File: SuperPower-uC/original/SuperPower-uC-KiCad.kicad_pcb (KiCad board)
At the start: 4 copper layers, 92.2 x 45.2 mm, 142 parts, among them J1 JST_PH_S2B_thru, J10 Conn_01x13_Male, J3 Conn_01x02_Male, J4 DNP/JST_ZH_S2B_thru, J5 DNP/JST_XH_S2B_thru, J6 Conn_01x02_Male, J7 Conn_01x14_Male, J8 Conn_01x14_Male, J9 Conn_01x13_Female, Q1 DMN2019UTS, Q10 2N7002A, Q11 2N7002A, Q12 DMP2035UVT, Q13 DMP2035UVT, Q14 DMP2035UVT, Q15 DMN3023L, Q2 Si3421DV, Q3 DMN3023L, Q4 2N7002A, Q5 DMP2035UVT, Q6 BSS84-7-F, Q7 S8050, Q8 S8050, Q9 2N7002A, SW1 DNP/SKRKAEE020, U1 AP9101CK6-AYTRG1, U10 TPS63070RNMT, U2 USB-C, U3 IP4220CZ6, U4 LTC4162EUFD-LAD, U5 RV-3028-C7, U6 CP2102N-A01-GQFN28, U7 ESP32-WROOM32, U8 TPS70933DRVT, U9 TPS63070RNMT

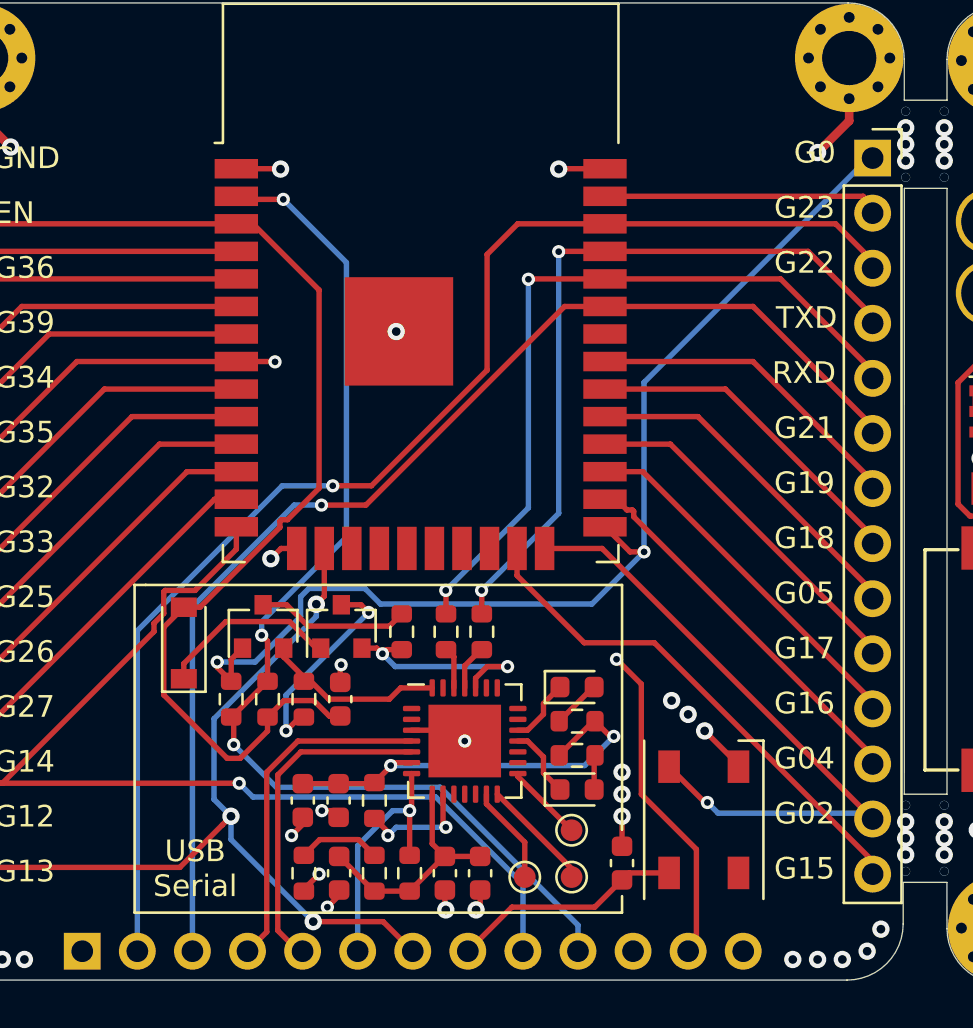
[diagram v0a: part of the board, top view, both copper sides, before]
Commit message: Changed silk text sizes
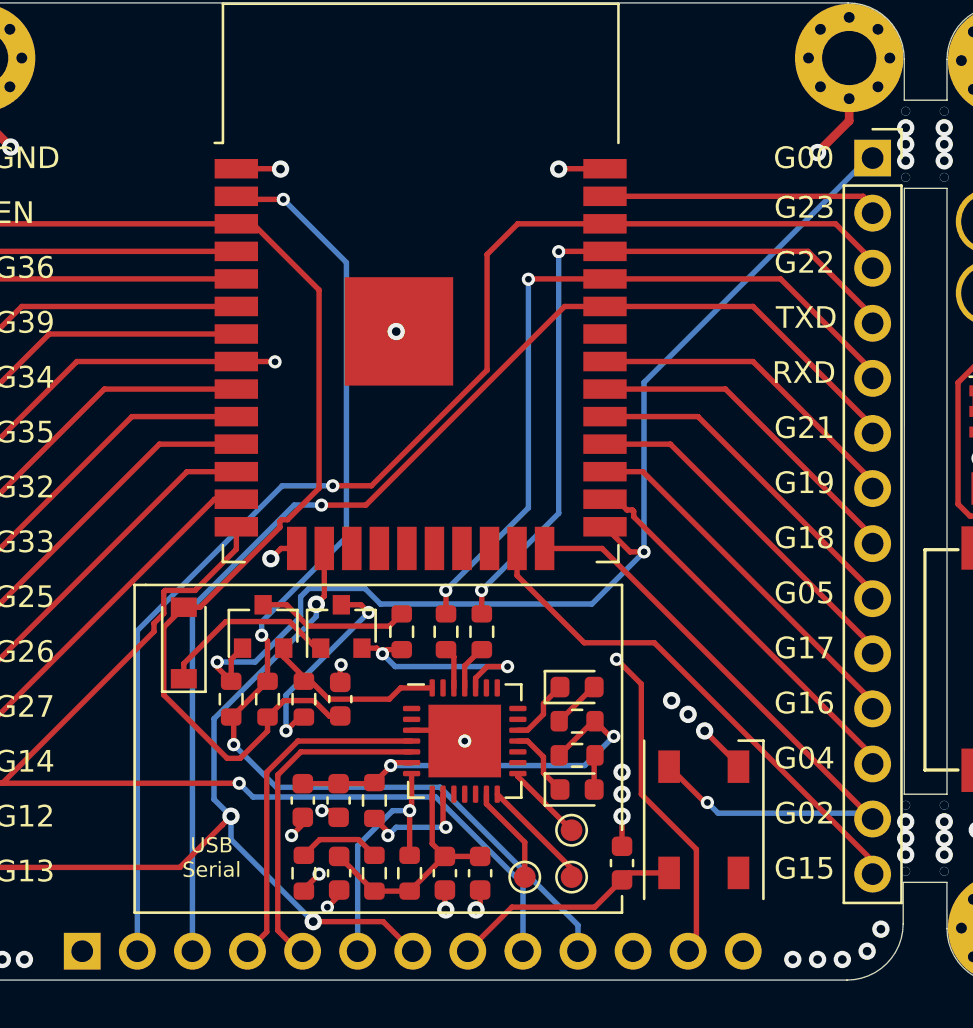
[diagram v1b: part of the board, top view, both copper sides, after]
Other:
- board text added: "G00"
- board text removed: "G0"
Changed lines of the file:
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@@
   (gr_line (start 173.355 76.454) (end 173.355 83.058) (layer F.SilkS) (width 0.12))
   (gr_text VIN (at 160.02 89.662) (layer B.SilkS)
-    (effects (font (size 0.5 0.5) (thickness 0.125)) (justify mirror))
+    (effects (font (size 0.7 0.7) (thickness 0.175)) (justify mirror))
   )
-  (gr_text GND (at 160.02 86.36) (layer B.SilkS)
-    (effects (font (size 0.5 0.5) (thickness 0.125)) (justify mirror))
+  (gr_text GND (at 160.147 86.36) (layer B.SilkS)
+    (effects (font (size 0.7 0.7) (thickness 0.175)) (justify mirror))
   )
-  (gr_text "Battery In" (at 186.69 82.804) (layer B.SilkS)
-    (effects (font (size 0.5 0.5) (thickness 0.125)) (justify mirror))
+  (gr_text "Battery In" (at 185.928 82.804) (layer B.SilkS)
+    (effects (font (size 0.7 0.7) (thickness 0.175)) (justify mirror))
   )
-  (gr_line (start 182.245 82.169) (end 188.722 82.169) (layer B.SilkS) (width 0.12))
-  (gr_line (start 193.167 95.25) (end 186.309 95.25) (layer B.SilkS) (width 0.12))
-  (gr_text "Battery Out" (at 190.246 89.027) (layer B.SilkS)
-    (effects (font (size 0.6 0.6) (thickness 0.125)) (justify mirror))
+  (gr_line (start 181.356 82.169) (end 188.722 82.169) (layer B.SilkS) (width 0.12))
+  (gr_line (start 193.167 95.25) (end 184.785 95.25) (layer B.SilkS) (width 0.12))
+  (gr_text "Battery Out" (at 189.865 88.773) (layer B.SilkS)
+    (effects (font (size 0.7 0.7) (thickness 0.175)) (justify mirror))
   )
-  (gr_line (start 161.29 91.313) (end 161.29 84.201) (layer B.SilkS) (width 0.12))
-  (gr_line (start 153.924 91.313) (end 161.29 91.313) (layer B.SilkS) (width 0.12))
+  (gr_line (start 163.576 91.313) (end 163.576 84.201) (layer B.SilkS) (width 0.12))
+  (gr_line (start 153.924 91.313) (end 163.576 91.313) (layer B.SilkS) (width 0.12))
   (gr_line (start 153.924 84.201) (end 153.924 91.313) (layer B.SilkS) (width 0.12))
-  (gr_line (start 161.29 84.201) (end 153.924 84.201) (layer B.SilkS) (width 0.12))
+  (gr_line (start 163.576 84.201) (end 153.924 84.201) (layer B.SilkS) (width 0.12))
   (gr_line (start 160.02 76.708) (end 160.02 80.899) (layer F.SilkS) (width 0.12))
   (gr_line (start 153.924 76.708) (end 160.02 76.708) (layer F.SilkS) (width 0.12))
@@
     (effects (font (size 0.7 0.7) (thickness 0.175)) (justify mirror))
   )
-  (gr_line (start 188.722 87.503) (end 182.245 87.503) (layer B.SilkS) (width 0.12))
+  (gr_line (start 188.722 87.503) (end 181.356 87.503) (layer B.SilkS) (width 0.12))
   (gr_line (start 188.722 82.169) (end 188.722 87.503) (layer B.SilkS) (width 0.12))
-  (gr_line (start 182.245 87.503) (end 182.245 82.169) (layer B.SilkS) (width 0.12))
-  (gr_line (start 193.167 95.25) (end 193.167 88.265) (layer B.SilkS) (width 0.12))
-  (gr_line (start 186.309 88.265) (end 186.309 95.25) (layer B.SilkS) (width 0.12))
-  (gr_line (start 193.167 88.265) (end 186.309 88.265) (layer B.SilkS) (width 0.12))
-  (gr_text "USB\nSerial" (at 114.046 116.205) (layer F.SilkS)
-    (effects (font (size 1 1) (thickness 0.15)))
+  (gr_line (start 181.356 87.503) (end 181.356 82.169) (layer B.SilkS) (width 0.12))
+  (gr_line (start 193.167 95.25) (end 193.167 88.138) (layer B.SilkS) (width 0.12))
+  (gr_line (start 184.785 88.138) (end 184.785 95.25) (layer B.SilkS) (width 0.12))
+  (gr_line (start 193.167 88.138) (end 184.785 88.138) (layer B.SilkS) (width 0.12))
+  (gr_text "USB\nSerial" (at 114.808 115.697) (layer F.SilkS)
+    (effects (font (size 0.7 0.7) (thickness 0.15)))
   )
   (gr_line (start 111.252 103.124) (end 111.76 103.124) (layer F.SilkS) (width 0.12))
@@
     (effects (font (size 1 1) (thickness 0.15)))
   )
-  (gr_text G0 (at 142.621 83.185) (layer F.SilkS)
+  (gr_text G00 (at 142.113 83.439) (layer F.SilkS)
     (effects (font (size 1 1) (thickness 0.15)))
   )
@@
   (gr_line (start 146.74596 78.87716) (end 146.74596 80.772) (layer Edge.Cuts) (width 0.05))
   (gr_line (start 148.717 80.772) (end 146.74596 80.772) (layer Edge.Cuts) (width 0.05))
-  (gr_text "Power In 5V-20V" (at 157.734 84.709) (layer B.SilkS)
-    (effects (font (size 0.5 0.5) (thickness 0.125)) (justify mirror))
+  (gr_text "Power In 5V-20V" (at 158.75 84.836) (layer B.SilkS)
+    (effects (font (size 0.7 0.7) (thickness 0.175)) (justify mirror))
   )
-  (gr_text GND (at 188.976 93.345) (layer B.SilkS)
-    (effects (font (size 0.5 0.5) (thickness 0.125)) (justify mirror))
+  (gr_text GND (at 188.595 93.345) (layer B.SilkS)
+    (effects (font (size 0.7 0.7) (thickness 0.175)) (justify mirror))
   )
-  (gr_text Battery+ (at 188.087 90.678) (layer B.SilkS)
-    (effects (font (size 0.5 0.5) (thickness 0.125)) (justify mirror))
+  (gr_text Battery+ (at 187.325 90.805) (layer B.SilkS)
+    (effects (font (size 0.7 0.7) (thickness 0.175)) (justify mirror))
   )
-  (gr_text Battery- (at 184.531 84.328) (layer B.SilkS)
-    (effects (font (size 0.5 0.5) (thickness 0.125)) (justify mirror))
+  (gr_text Battery- (at 183.896 84.328) (layer B.SilkS)
+    (effects (font (size 0.7 0.7) (thickness 0.175)) (justify mirror))
   )
-  (gr_text Battery+ (at 184.531 86.36) (layer B.SilkS)
-    (effects (font (size 0.5 0.5) (thickness 0.125)) (justify mirror))
+  (gr_text Battery+ (at 183.896 86.36) (layer B.SilkS)
+    (effects (font (size 0.7 0.7) (thickness 0.175)) (justify mirror))
   )
   (gr_text SCL (at 158.369 117.673429 90) (layer B.SilkS)

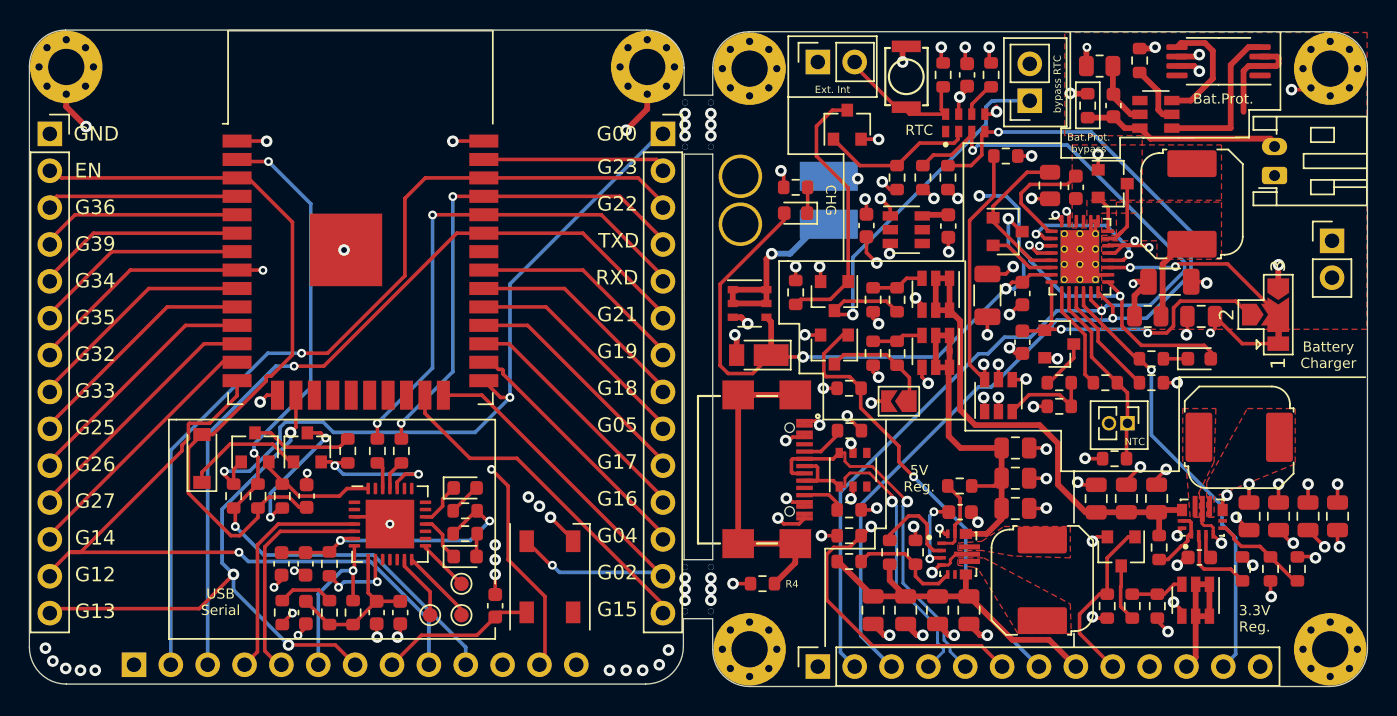
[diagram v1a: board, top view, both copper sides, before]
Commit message: Made designators visible (not all but most)
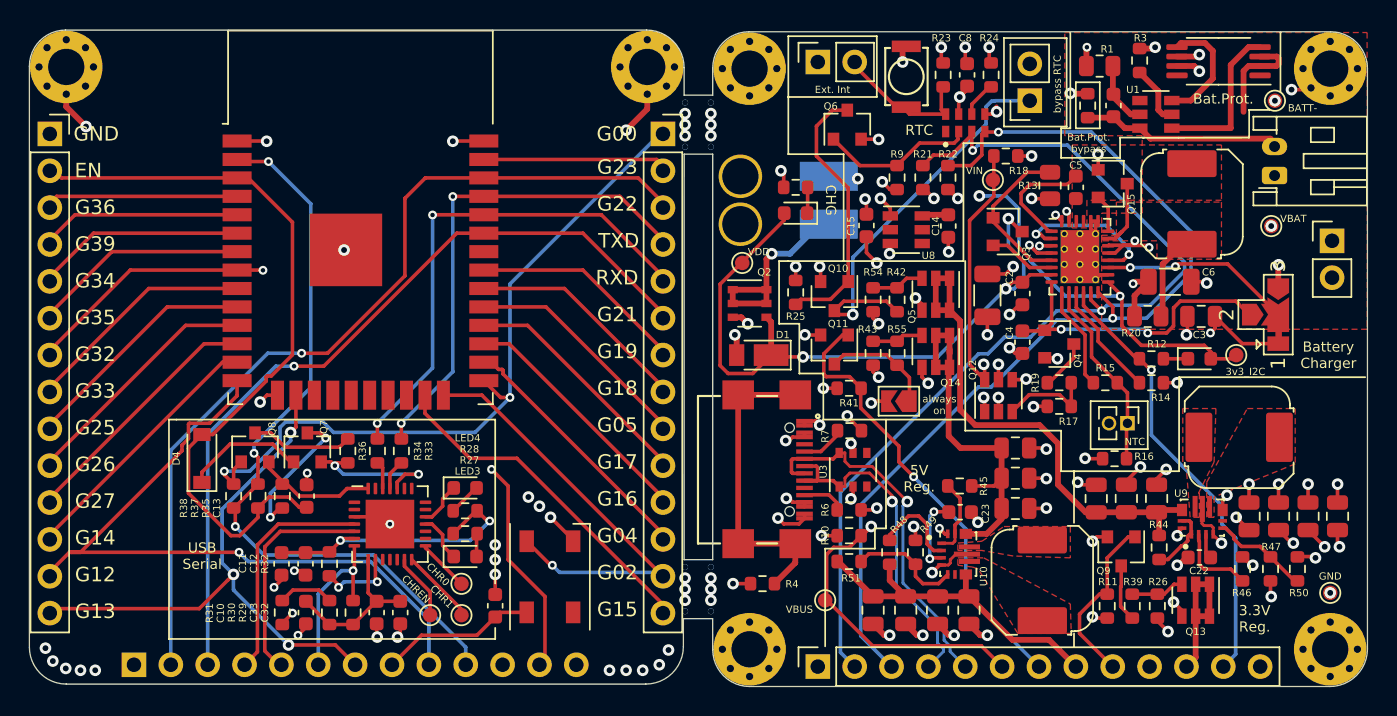
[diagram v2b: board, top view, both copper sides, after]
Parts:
- added 3v3_I2C: 3V3_I2C, TestPoint:TestPoint_Pad_D1.0mm, F.Cu at (184.8, 98.7)
- added BATT-: BATT-, TestPoint:TestPoint_Pad_D1.0mm, F.Cu at (187.5, 81.2)
- added GND: GND, TestPoint:TestPoint_Pad_D1.0mm, F.Cu at (191.3, 115.1)
- added VBAT: VBAT, TestPoint:TestPoint_Pad_D1.0mm, F.Cu at (187.2, 89.8)
- added VBUS: TestPoint, TestPoint:TestPoint_Pad_D1.0mm, F.Cu at (156.5, 115.6)
- added VDD: TestPoint, TestPoint:TestPoint_Pad_D1.0mm, F.Cu at (150.7, 92.3)
- added VIN: VOUT, TestPoint:TestPoint_Pad_D1.0mm, F.Cu at (168.0, 86.6)
- renumbered TP30 to CHR0, TP31 to CHR1, TP29 to CHREN
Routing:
- net /Charging Module/3v3_I2C: track 35.1 -> 37.0 mm
- net GND: vias 99 -> 100
- net /Battery Module/VBAT: vias 4 -> 5
- net -BATT: vias 0 -> 1
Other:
- board text added: "always on"

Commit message: Fix designator sizes and placements
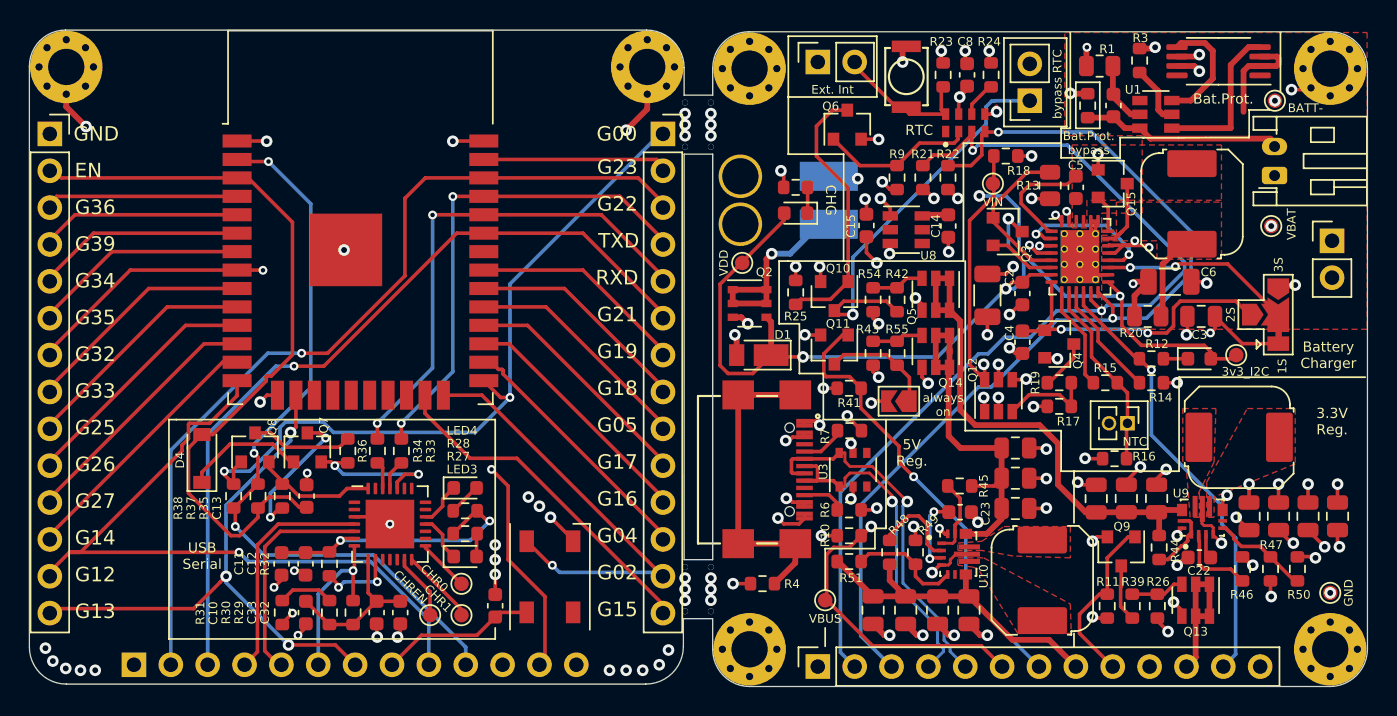
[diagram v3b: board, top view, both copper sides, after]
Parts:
- moved VIN 0.25 mm to (168.0, 86.9)
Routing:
- net GND: track 125.3 -> 124.3 mm
- net /EN_5V_1: track 40.0 -> 39.2 mm

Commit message: Add revision and date
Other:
- board text added: "v1.00 (2021-01)"

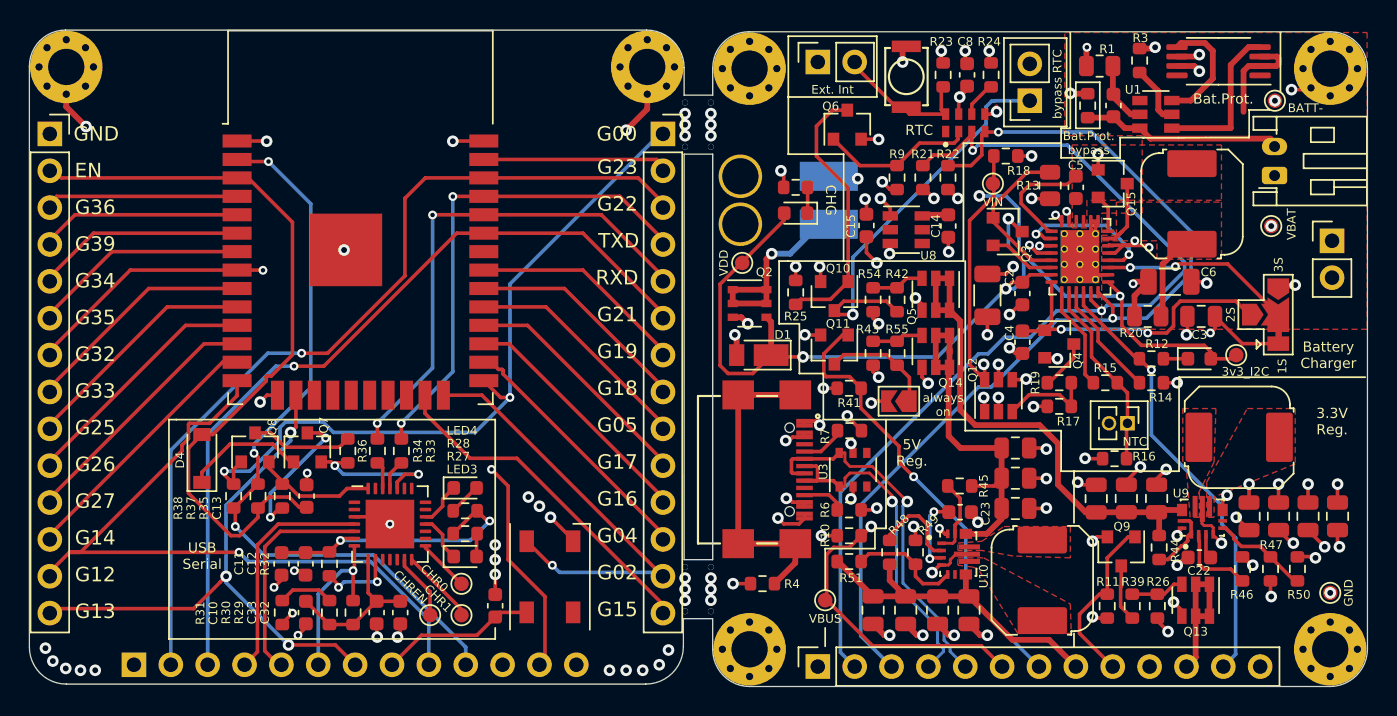
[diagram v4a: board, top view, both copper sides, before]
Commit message: Swapped GND Pins on the interface connector
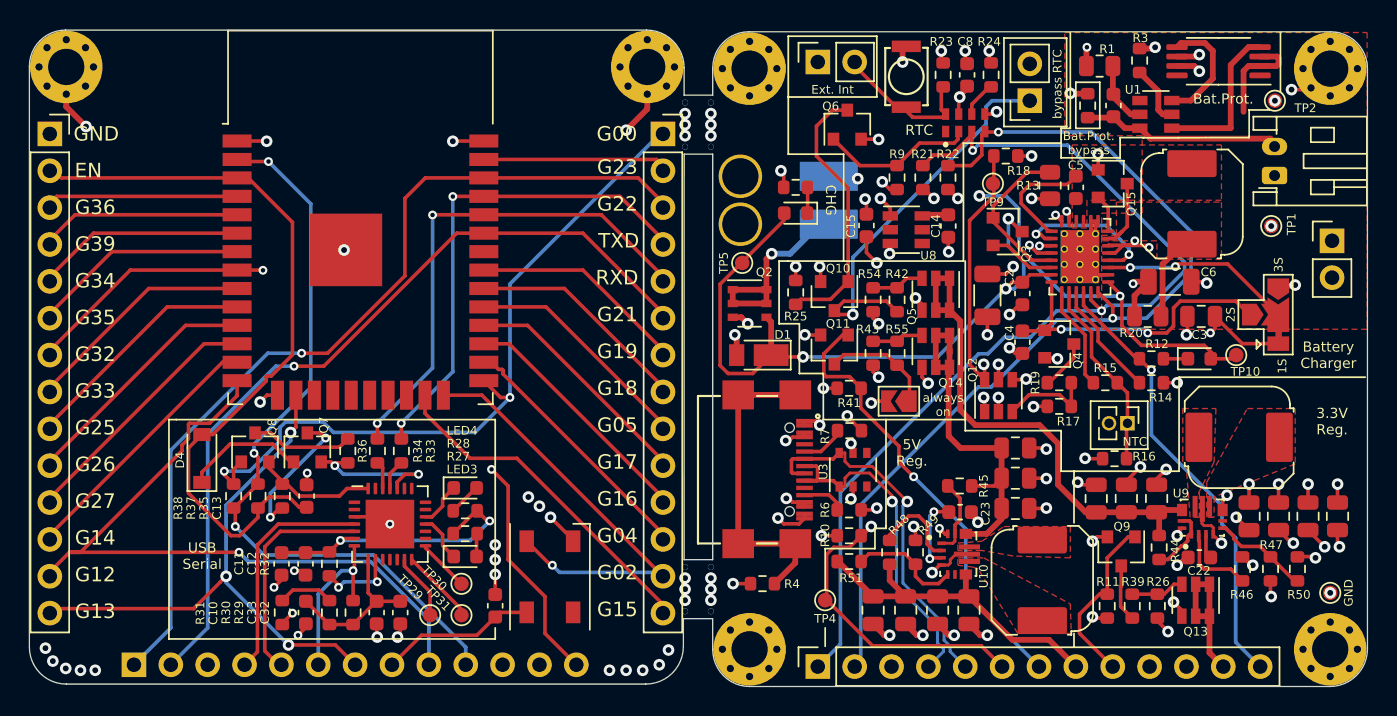
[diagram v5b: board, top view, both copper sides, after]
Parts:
- renumbered VBAT to TP1, 3v3_I2C to TP10, BATT- to TP2, CHREN to TP29, CHR0 to TP30, CHR1 to TP31, VBUS to TP4, VDD to TP5, VIN to TP9
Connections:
- J10 pad 1: GND -> /SCL
- J10 pad 11: /3v3 -> GND
- J10 pad 12: /~SMBALERT -> /3v3
- J10 pad 13: GND -> /~SMBALERT
- J10 pad 2: /SCL -> /SDA
- J10 pad 3: /SDA -> GND
- J9 pad 1: GND -> /SCL_1
- J9 pad 11: /3v3_1 -> GND
- J9 pad 12: /~SMBALERT_1 -> /3v3_1
- J9 pad 13: GND -> /~SMBALERT_1
- J9 pad 2: /SCL_1 -> /SDA_1
- J9 pad 3: /SDA_1 -> GND
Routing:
- net /SCL_1: track 60.4 -> 61.4 mm
- net /SDA_1: track 55.4 -> 56.4 mm
- net /~SMBALERT_1: track 53.6 -> 54.3 mm
- net /SDA: track 67.9 -> 67.2 mm
- net /3v3_1: track 0.00 -> 0.54 mm

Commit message: Fixed all review actions from ManraRayDeeJay
https://github.com/Informaticore/SuperPower/issues/69
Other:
- board text added: "Power In 5V-16V"
- board text removed: "Power In 5V-20V"
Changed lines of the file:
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@@
   (layers
     (0 F.Cu signal)
-    (1 In1.Cu signal)
+    (1 In1.Cu power)
     (2 In2.Cu signal)
     (31 B.Cu signal)
@@
   (gr_line (start 146.74596 78.87716) (end 146.74596 80.772) (layer Edge.Cuts) (width 0.05))
   (gr_line (start 148.717 80.772) (end 146.74596 80.772) (layer Edge.Cuts) (width 0.05))
-  (gr_text "Power In 5V-20V" (at 159.258 84.836) (layer B.SilkS)
+  (gr_text "Power In 5V-16V" (at 159.258 84.836) (layer B.SilkS)
     (effects (font (size 0.7 0.7) (thickness 0.175)) (justify mirror))
   )
@@
     (polygon
       (pts
-        (xy 168.783 92.172774) (xy 158.369 92.172774) (xy 158.369 84.806774) (xy 153.924 84.806774) (xy 153.924 76.551774)
-        (xy 168.783 76.551774)
+        (xy 168.021 81.153) (xy 168.021 88.773) (xy 158.369 88.773) (xy 156.21 86.868) (xy 153.924 84.806774)
+        (xy 153.924 76.551774) (xy 161.3535 76.551774) (xy 162.178602 76.555019) (xy 165.735 79.121)
       )
     )
